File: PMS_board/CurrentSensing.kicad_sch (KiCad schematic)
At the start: 4 parts, among them U26 INA186A3IDCK, U3 MCP3204T-CI/ST

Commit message: How did our footprints get this geeked???
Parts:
- C40: footprint Capacitor_SMD:C_0603_1608Metric -> Capacitor_SMD:C_0603_1608Metric_Pad1.08x0.95mm_HandSolder
- R36: footprint Package_SON:WSON-8-1EP_6x5mm_P1.27mm_EP3.4x4mm -> (none)
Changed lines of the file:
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@@
 			)
 		)
-		(property "Footprint" "Package_SON:WSON-8-1EP_6x5mm_P1.27mm_EP3.4x4mm"
+		(property "Footprint" ""
 			(at 68.072 105.41 90)
 			(hide yes)
@@
 			)
 		)
-		(property "Footprint" "Capacitor_SMD:C_0603_1608Metric"
+		(property "Footprint" "Capacitor_SMD:C_0603_1608Metric_Pad1.08x0.95mm_HandSolder"
 			(at 80.3148 92.71 0)
 			(hide yes)

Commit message: Changed relay out for PMOS power switching
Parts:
- R36: footprint (none) -> Footprints:ShuntSMD_BVT-M-R001-1.0
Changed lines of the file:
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@@
 			)
 		)
-		(property "Footprint" ""
+		(property "Footprint" "Footprints:ShuntSMD_BVT-M-R001-1.0"
 			(at 68.072 105.41 90)
 			(hide yes)
@@
 			)
 		)
-		(property "Datasheet" ""
+		(property "Datasheet" "https://www.digikey.com/en/products/detail/isabellenhuette-usa/BVT-M-R001-1-0/16627455"
 			(at 69.85 105.41 0)
 			(hide yes)

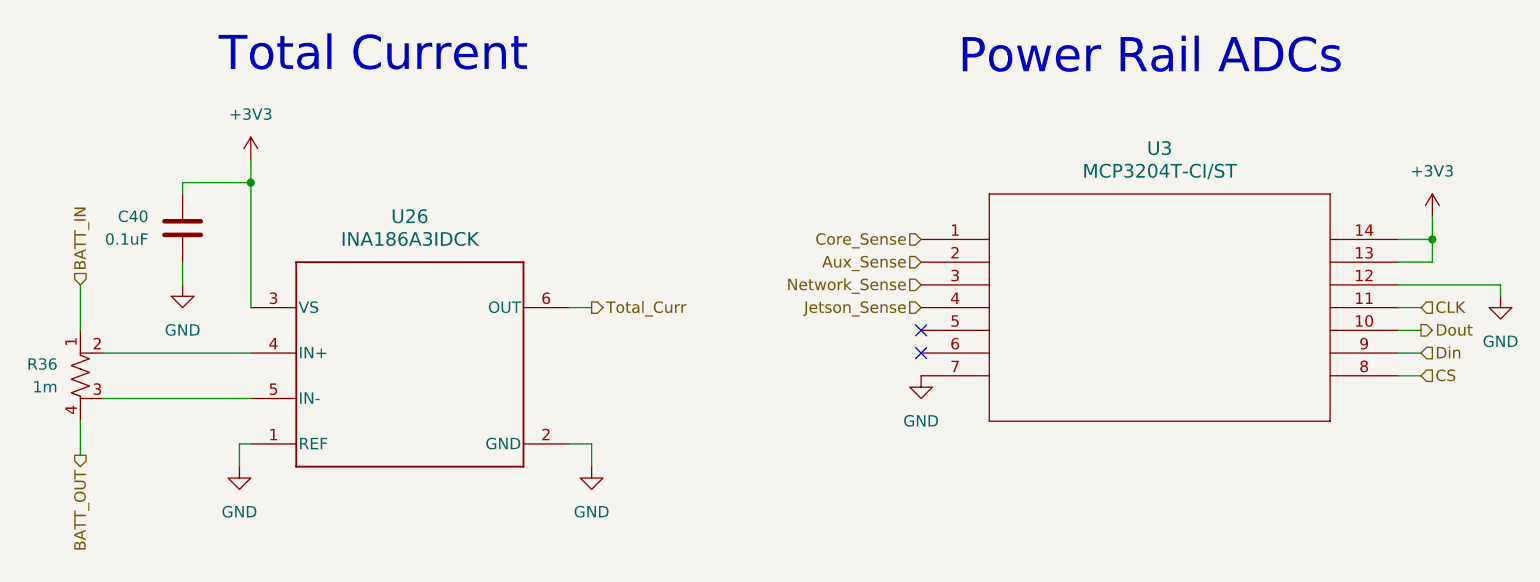
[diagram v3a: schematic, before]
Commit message: New current sensor using old op amp
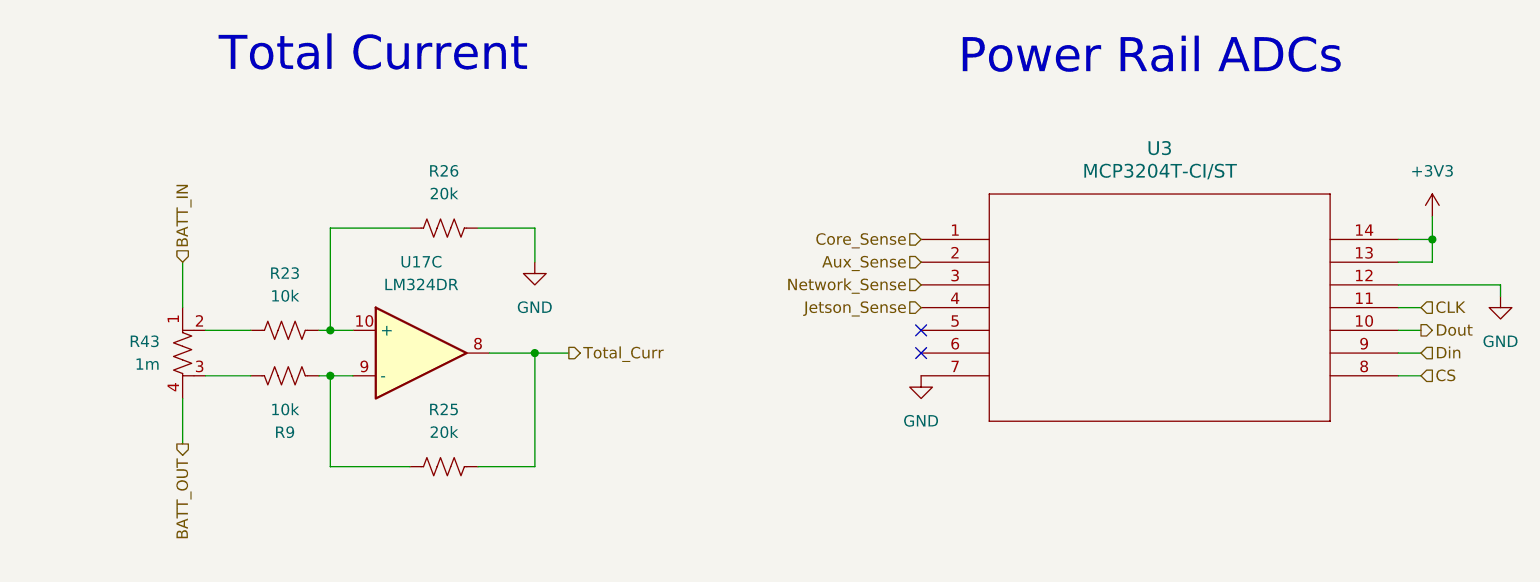
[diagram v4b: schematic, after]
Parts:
- removed C40: 0.1uF, Capacitor_SMD:C_0603_1608Metric_Pad1.08x0.95mm_HandSolder, symbol Device:C
- removed R36: 1m, Footprints:ShuntSMD_BVT-M-R001-1.0, symbol Device:R_Shunt_US
- removed U26: INA186A3IDCK, INA186A3IDCK:SO8_DCK_TEX, symbol Symbols:INA186A2QDCKRQ1
- added R23, R9: 10k, symbol Device:R_US
- added R25, R26: 20k, symbol Device:R_US
- added R43: 1m, Footprints:ShuntSMD_BVT-M-R001-1.0, symbol Device:R_Shunt_US
- added U17: LM324DR, Package_SO:SOIC-14_3.9x8.7mm_P1.27mm, symbol Amplifier_Operational:Opamp_Quad
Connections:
- net BATT_IN: now also R43.1
- net BATT_OUT: now also R43.4
- net GND: now also R26.2
- net Total_Curr: now also R25.2, U17.8
- new net: R43.3, R9.1
- new net: R25.1, R9.2, U17.9 (-)
- new net: R23.2, R26.1, U17.10 (+)
- new net: R23.1, R43.2

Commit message: Fixed references
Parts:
- renumbered R43 to R83, R23 to R84, R9 to R85, R26 to R86, R25 to R87, U17 to U2, U3 to U20
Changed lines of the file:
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@@
 		(in_pos_files yes)
 		(dnp no)
-		(property "Reference" "R9"
+		(property "Reference" "R85"
 			(at 92.71 111.76 90)
 			(show_name no)
@@
 			(project "PMS_board"
 				(path "/282246b0-e0d8-4997-b3ee-58bf10355d52/9ae2dcd5-51ae-42d9-a1ef-fc7cd7fabc7d"
-					(reference "R9")
+					(reference "R85")
 					(unit 1)
 				)
@@
 		(dnp no)
 		(fields_autoplaced yes)
-		(property "Reference" "U17"
+		(property "Reference" "U2"
 			(at 107.95 92.71 0)
 			(show_name no)
@@
 			(project "PMS_board"
 				(path "/282246b0-e0d8-4997-b3ee-58bf10355d52/9ae2dcd5-51ae-42d9-a1ef-fc7cd7fabc7d"
-					(reference "U17")
+					(reference "U2")
 					(unit 3)
 				)
@@
 		(dnp no)
 		(fields_autoplaced yes)
-		(property "Reference" "#PWR092"
+		(property "Reference" "#PWR095"
 			(at 220.98 91.44 0)
 			(hide yes)
@@
 			(project "PMS_board"
 				(path "/282246b0-e0d8-4997-b3ee-58bf10355d52/9ae2dcd5-51ae-42d9-a1ef-fc7cd7fabc7d"
-					(reference "#PWR092")
+					(reference "#PWR095")
 					(unit 1)
 				)
@@
 		(in_pos_files yes)
 		(dnp no)
-		(property "Reference" "R26"
+		(property "Reference" "R86"
 			(at 110.49 82.55 90)
 			(show_name no)
@@
 			(project "PMS_board"
 				(path "/282246b0-e0d8-4997-b3ee-58bf10355d52/9ae2dcd5-51ae-42d9-a1ef-fc7cd7fabc7d"
-					(reference "R26")
+					(reference "R86")
 					(unit 1)
 				)
@@
 		(in_pos_files yes)
 		(dnp no)
-		(property "Reference" "R25"
+		(property "Reference" "R87"
 			(at 110.49 109.22 90)
 			(show_name no)
@@
 			(project "PMS_board"
 				(path "/282246b0-e0d8-4997-b3ee-58bf10355d52/9ae2dcd5-51ae-42d9-a1ef-fc7cd7fabc7d"
-					(reference "R25")
+					(reference "R87")
 					(unit 1)
 				)
@@
 		(dnp no)
 		(fields_autoplaced yes)
-		(property "Reference" "#PWR012"
+		(property "Reference" "#PWR093"
 			(at 120.65 99.06 0)
 			(hide yes)
@@
 			(project "PMS_board"
 				(path "/282246b0-e0d8-4997-b3ee-58bf10355d52/9ae2dcd5-51ae-42d9-a1ef-fc7cd7fabc7d"
-					(reference "#PWR012")
+					(reference "#PWR093")
 					(unit 1)
 				)
@@
 		(dnp no)
 		(fields_autoplaced yes)
-		(property "Reference" "#PWR091"
+		(property "Reference" "#PWR096"
 			(at 228.6 102.87 0)
 			(hide yes)
@@
 			(project "PMS_board"
 				(path "/282246b0-e0d8-4997-b3ee-58bf10355d52/9ae2dcd5-51ae-42d9-a1ef-fc7cd7fabc7d"
-					(reference "#PWR091")
+					(reference "#PWR096")
 					(unit 1)
 				)
@@
 		(dnp no)
 		(fields_autoplaced yes)
-		(property "Reference" "#PWR090"
+		(property "Reference" "#PWR094"
 			(at 163.83 111.76 0)
 			(hide yes)
@@
 			(project "PMS_board"
 				(path "/282246b0-e0d8-4997-b3ee-58bf10355d52/9ae2dcd5-51ae-42d9-a1ef-fc7cd7fabc7d"
-					(reference "#PWR090")
+					(reference "#PWR094")
 					(unit 1)
 				)
@@
 		(dnp no)
 		(fields_autoplaced yes)
-		(property "Reference" "R43"
+		(property "Reference" "R83"
 			(at 78.74 101.5999 0)
 			(show_name no)
@@
 			(project "PMS_board"
 				(path "/282246b0-e0d8-4997-b3ee-58bf10355d52/9ae2dcd5-51ae-42d9-a1ef-fc7cd7fabc7d"
-					(reference "R43")
+					(reference "R83")
 					(unit 1)
 				)
@@
 		(dnp no)
 		(fields_autoplaced yes)
-		(property "Reference" "U3"
+		(property "Reference" "U20"
 			(at 190.5 80.01 0)
 			(show_name no)
@@
 			(project "PMS_board"
 				(path "/282246b0-e0d8-4997-b3ee-58bf10355d52/9ae2dcd5-51ae-42d9-a1ef-fc7cd7fabc7d"
-					(reference "U3")
+					(reference "U20")
 					(unit 1)
 				)
@@
 		(in_pos_files yes)
 		(dnp no)
-		(property "Reference" "R23"
+		(property "Reference" "R84"
 			(at 92.71 93.98 90)
 			(show_name no)
@@
 			(project "PMS_board"
 				(path "/282246b0-e0d8-4997-b3ee-58bf10355d52/9ae2dcd5-51ae-42d9-a1ef-fc7cd7fabc7d"
-					(reference "R23")
+					(reference "R84")
 					(unit 1)
 				)

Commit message: Footprints for connectors and new resistors
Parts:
- R84, R85, R86, R87: footprint (none) -> Resistor_SMD:R_0603_1608Metric_Pad0.98x0.95mm_HandSolder
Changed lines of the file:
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@@
 			)
 		)
-		(property "Footprint" ""
+		(property "Footprint" "Resistor_SMD:R_0603_1608Metric_Pad0.98x0.95mm_HandSolder"
 			(at 92.964 106.426 90)
 			(hide yes)
@@
 			)
 		)
-		(property "Footprint" ""
+		(property "Footprint" "Resistor_SMD:R_0603_1608Metric_Pad0.98x0.95mm_HandSolder"
 			(at 110.744 87.884 90)
 			(hide yes)
@@
 			)
 		)
-		(property "Footprint" ""
+		(property "Footprint" "Resistor_SMD:R_0603_1608Metric_Pad0.98x0.95mm_HandSolder"
 			(at 110.744 114.554 90)
 			(hide yes)
@@
 			)
 		)
-		(property "Footprint" ""
+		(property "Footprint" "Resistor_SMD:R_0603_1608Metric_Pad0.98x0.95mm_HandSolder"
 			(at 92.964 99.314 90)
 			(hide yes)

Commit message: Refix Review Work
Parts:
- R83: footprint Footprints:ShuntSMD_BVT-M-R001-1.0 -> Current_Sense:ShuntSMD_BVT-M-R001-1.0
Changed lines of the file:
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@@
 			)
 		)
-		(property "Footprint" "Footprints:ShuntSMD_BVT-M-R001-1.0"
+		(property "Footprint" "Current_Sense:ShuntSMD_BVT-M-R001-1.0"
 			(at 79.502 102.87 90)
 			(hide yes)

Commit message: Fixed Shunt symbol
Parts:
- removed R83: 1m, Current_Sense:ShuntSMD_BVT-M-R001-1.0, symbol Device:R_Shunt_US
- added R3: 1m, Current_Sense:ShuntSMD_BVT-M-R001-1.0, symbol Device:R_US
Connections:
- net BATT_IN: now also R84.1, R3.1
- net BATT_OUT: now also R85.1, R3.2
